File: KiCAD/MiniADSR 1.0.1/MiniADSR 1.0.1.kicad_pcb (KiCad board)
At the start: 2 copper layers, 105 x 128.5 mm, 50 parts, among them J1 INPUT, J2 OUTPUT, J3 JST_BUS, J4 ControlBoard_Pins, J5 IDC_BUS, J6 MainBoard_Pins, Q1 BC547, Q2 BC547, Q3 BC547, U1 LM555, U2 TL072

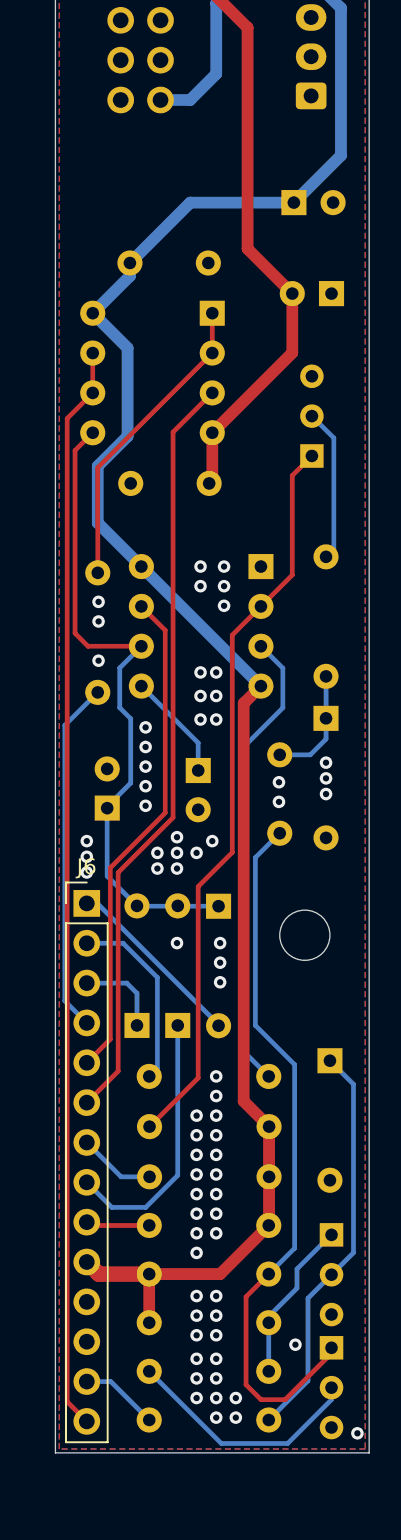
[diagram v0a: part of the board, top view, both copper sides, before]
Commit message: Added v1.0.1 for minor corrections on first version
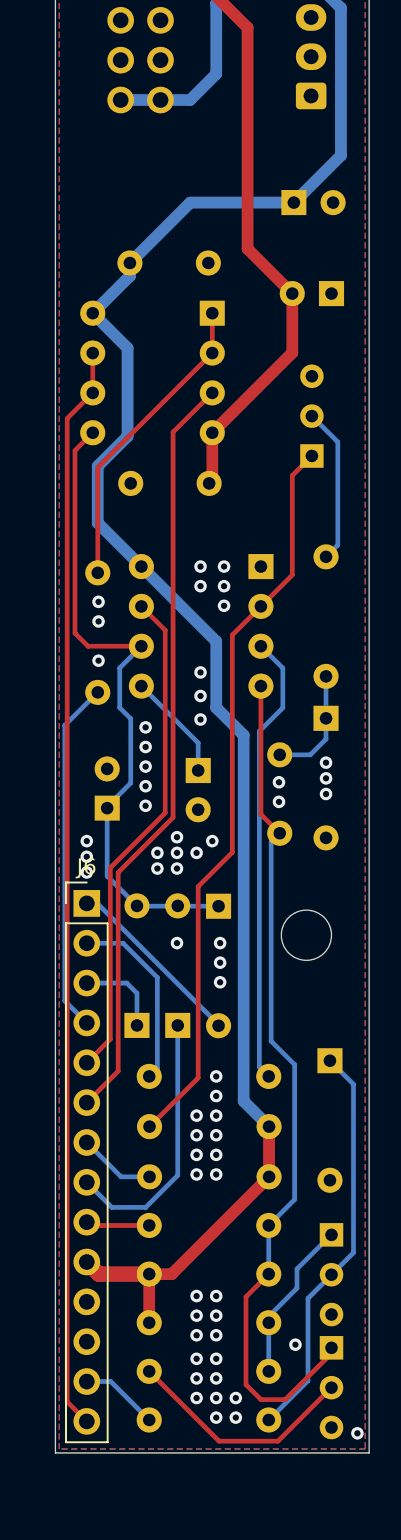
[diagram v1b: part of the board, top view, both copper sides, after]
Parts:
- C2: value *10uF -> 10uF
- C3: value 100uF -> 1uF*
- D1, D2, D3, D4, D5: value 4148 -> 1N4148
- POT_SUSTAIN1: value 1M -> 10K
- U1: value LM555 -> LM555xN
- moved REF** 0.10 mm to (151.0, 122.5)
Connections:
- R7 pad 1: +12V -> Net-(C1-Pad2)
- U1 pad 4: +12V -> Net-(C1-Pad2)
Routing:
- net Net-(C1-Pad2): track 45.5 -> 54.6 mm
- net Net-(R8-Pad1): track 29.7 -> 28.9 mm
- net Net-(Q2-Pad2): track 15.4 -> 14.9 mm
- net GND2: vias 68 -> 58

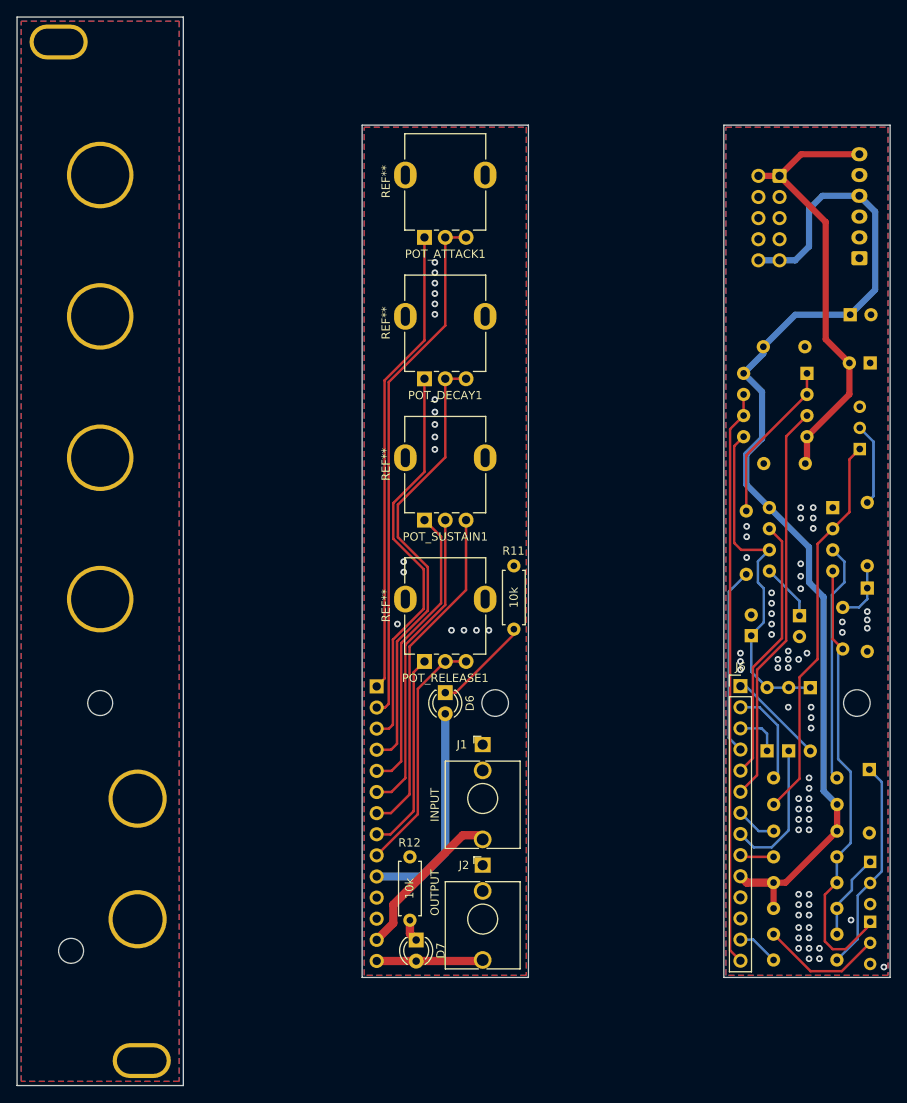
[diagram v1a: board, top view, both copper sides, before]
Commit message: Flipped power connectors for v1.0.1
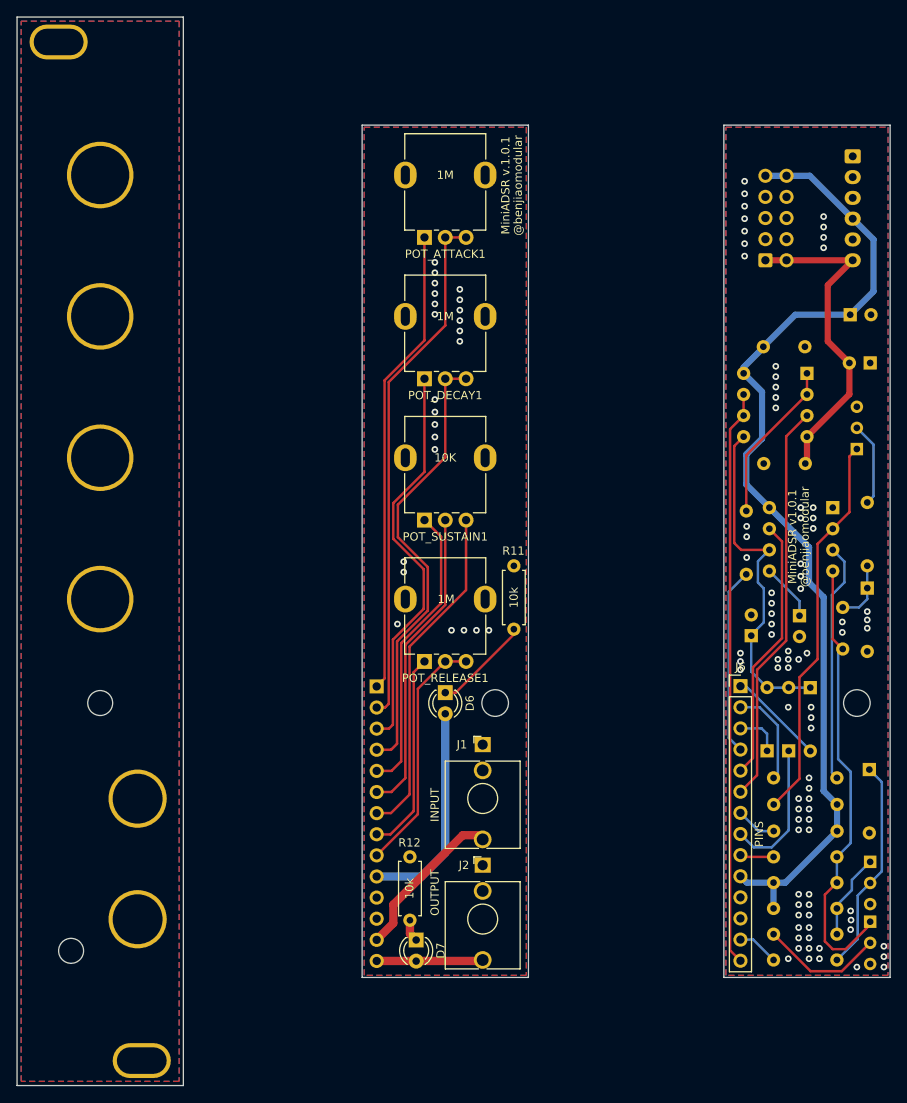
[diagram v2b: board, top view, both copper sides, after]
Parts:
- moved J3 12.3 mm to (150.5, 56.8), turned to 270 degrees
- moved J5 10.3 mm to (140.0, 69.2), turned to 0 degrees
- moved Q3 0.35 mm to (151.0, 92.0)
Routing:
- net -12V: track 53.5 -> 39.5 mm
- net +12V: track 129.4 -> 121.5 mm
- net GND2: vias 58 -> 80
- net GND1: vias 18 -> 24
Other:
- board text added: "MiniADSR v.1.0.1"
- board text added: "MiniADSR v1.0.1"
- board text added: "PINS"
- board text added: "SOCKETS"
